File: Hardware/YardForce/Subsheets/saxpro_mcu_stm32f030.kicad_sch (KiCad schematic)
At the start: 9 parts, among them U3 STM32F030RCTx

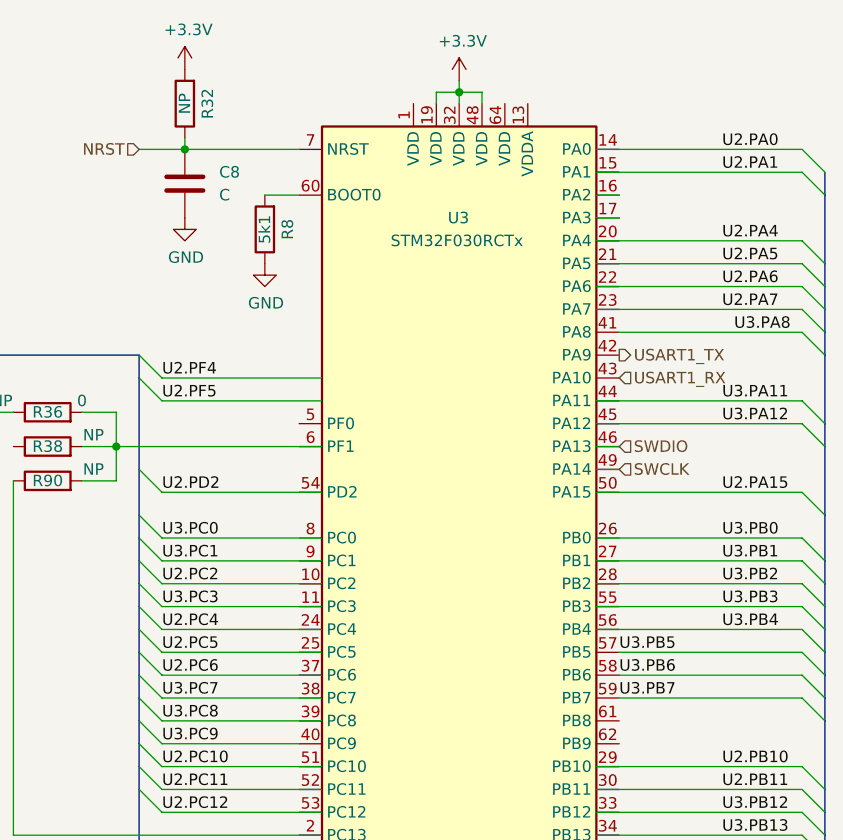
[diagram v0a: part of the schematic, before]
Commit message: Add touch panel
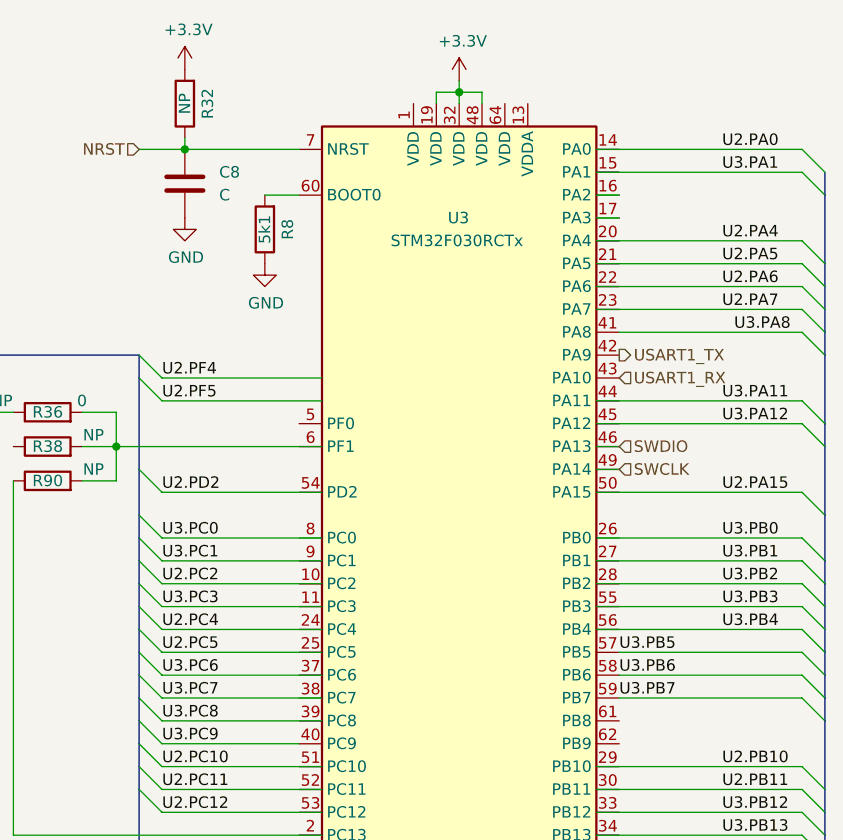
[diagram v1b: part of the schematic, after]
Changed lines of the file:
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@@
     (effects (font (size 1.27 1.27)) (justify left bottom))
   )
-  (label "U2.PC6" (at 93.98 106.68 0)
+  (label "U3.PC6" (at 93.98 106.68 0)
     (effects (font (size 1.27 1.27)) (justify left bottom))
   )
@@
     (effects (font (size 1.27 1.27)) (justify left bottom))
   )
-  (label "U2.PA1" (at 156.21 50.8 0)
+  (label "U3.PA1" (at 156.21 50.8 0)
     (effects (font (size 1.27 1.27)) (justify left bottom))
   )

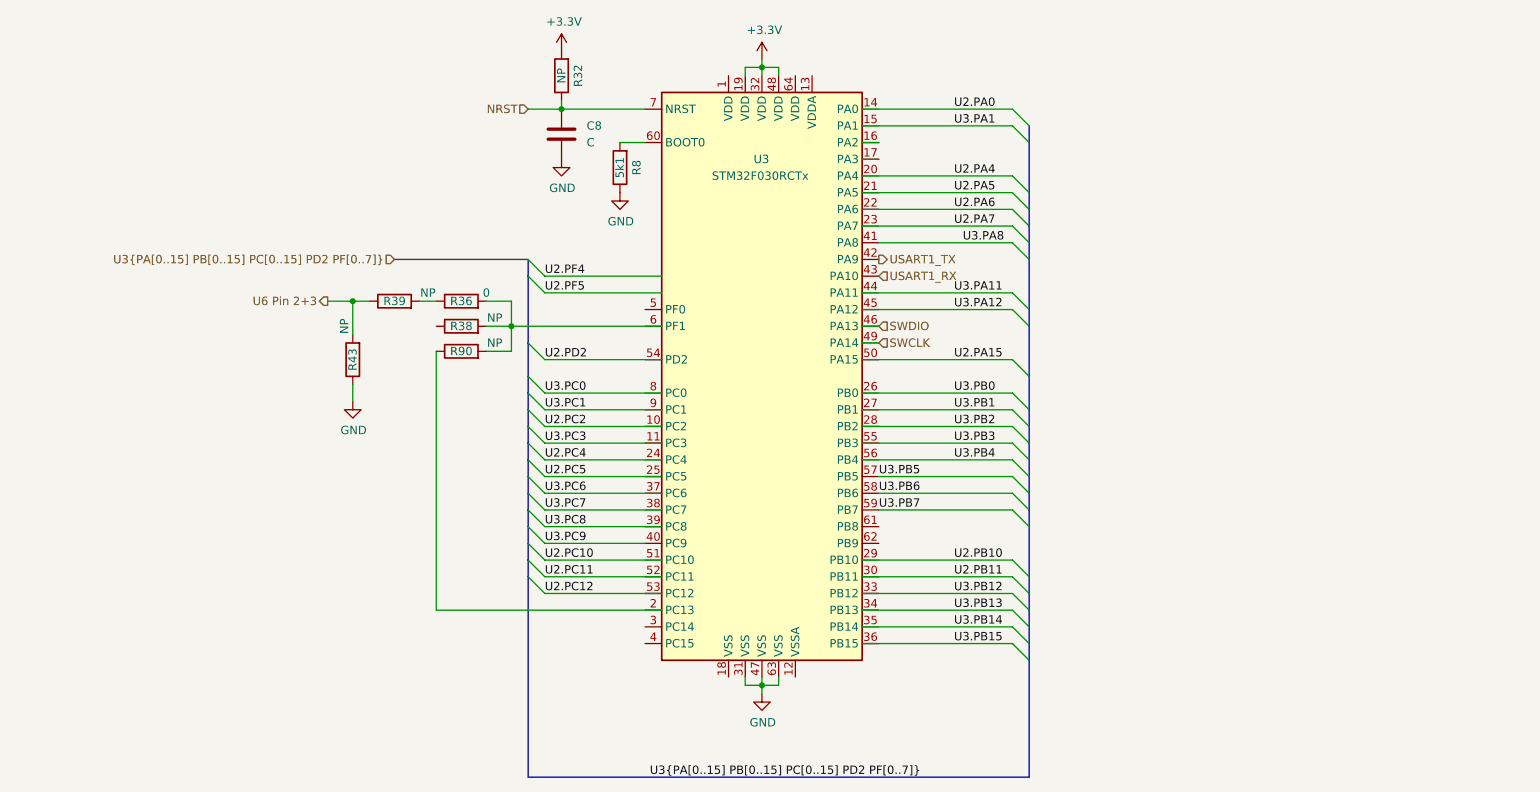
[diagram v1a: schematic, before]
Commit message: Add flash and some cleanup
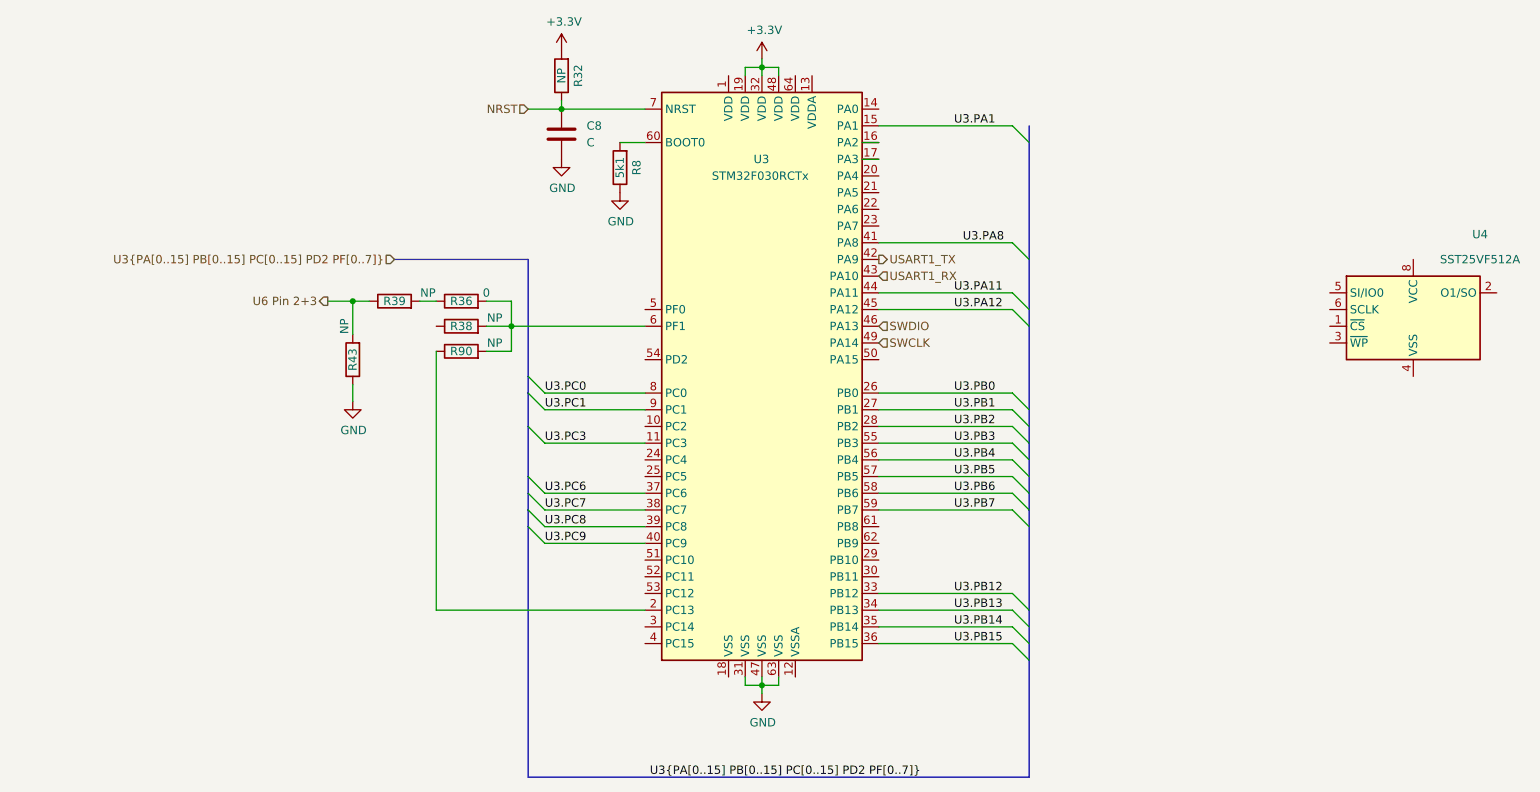
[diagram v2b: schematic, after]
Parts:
- added U4: SST25VF512A, Package_SO:SOP-8_3.9x4.9mm_P1.27mm, symbol Memory_Flash:GD25D05CT
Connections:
- net U3.PA1: now also U3.15 (PA1)
- net U3.PA11: now also U3.44 (PA11)
- net U3.PA12: now also U3.45 (PA12)
- net U3.PB0: now also U3.26 (PB0)
- net U3.PB1: now also U3.27 (PB1)
- net U3.PB12: now also U3.33 (PB12)
- net U3.PB13: now also U3.34 (PB13)
- net U3.PB14: now also U3.35 (PB14)
- net U3.PB15: now also U3.36 (PB15)
- net U3.PB2: now also U3.28 (PB2)
- net U3.PB3: now also U3.55 (PB3)
- net U3.PB4: now also U3.56 (PB4)
- net U3.PC0: now also U3.8 (PC0)
- net U3.PC1: now also U3.9 (PC1)
- net U3.PC3: now also U3.11 (PC3)
- net U3.PC6: now also U3.37 (PC6)
- net U3.PC7: now also U3.38 (PC7)
- net U3.PC8: now also U3.39 (PC8)
- net at R90.1: now also U3.2 (PC13)
- net at R36.2, R38.2, R90.2: now also U3.6 (PF1)
